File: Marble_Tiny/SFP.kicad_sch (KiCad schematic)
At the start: 73 parts, among them J1 TYCO_1888247-1, J11 TYCO_1888247-1, J12 TYCO_1888247-1, J13 TYCO_1888247-1, J8 2180739-1, J9 2180739-1, U17 TCA9535RTWR, U19 TCA9535RTWR, U26 PCA9546ARGV

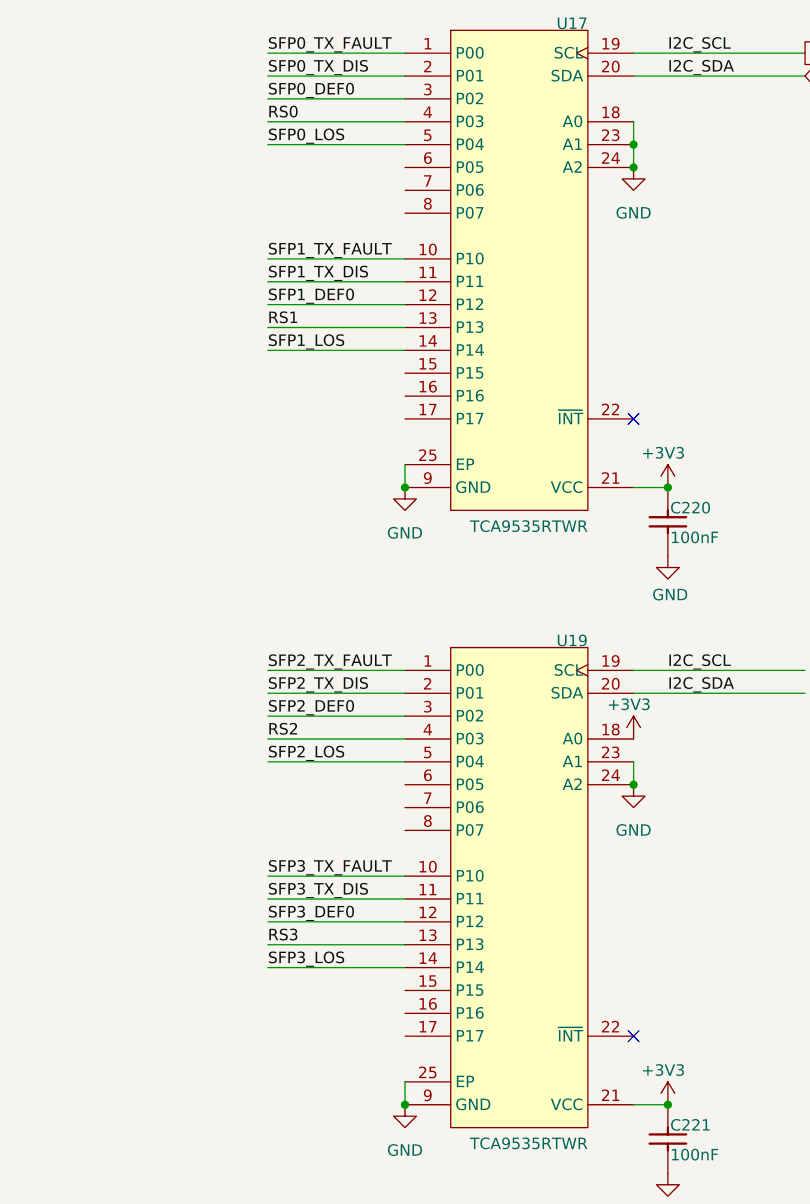
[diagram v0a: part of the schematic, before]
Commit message: fixed ERCs; added test points; added WP switch
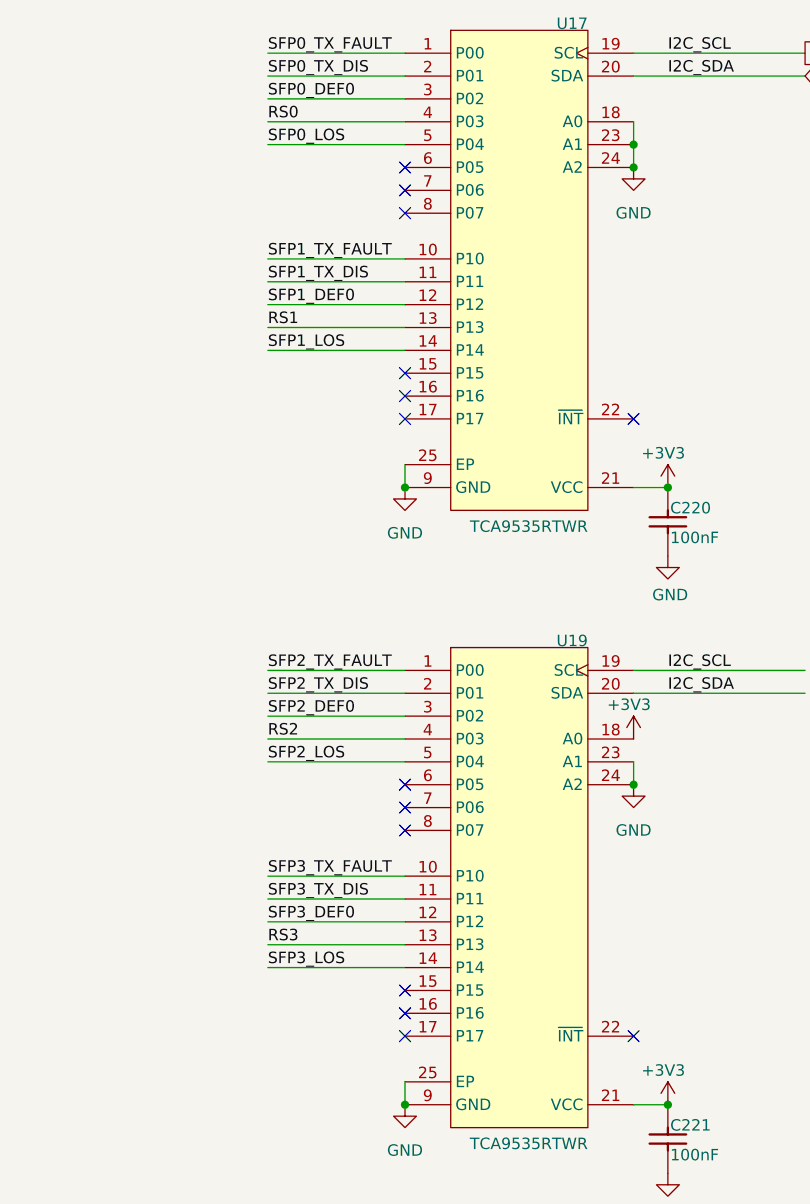
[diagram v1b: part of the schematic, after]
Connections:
- no-connect marks 3 -> 15
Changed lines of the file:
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@@
+	)
+	(no_connect
+		(at 323.85 115.57)
+	)
+	(no_connect
+		(at 323.85 110.49)
 	)
 	(no_connect
@@
 	)
 	(no_connect
+		(at 323.85 64.77)
+	)
+	(no_connect
+		(at 323.85 41.91)
+	)
+	(no_connect
+		(at 323.85 69.85)
+	)
+	(no_connect
+		(at 323.85 46.99)
+	)
+	(no_connect
+		(at 323.85 113.03)
+	)
+	(no_connect
 		(at 349.25 138.43)
+	)
+	(no_connect
+		(at 323.85 67.31)
+	)
+	(no_connect
+		(at 323.85 133.35)
+	)
+	(no_connect
+		(at 323.85 135.89)
+	)
+	(no_connect
+		(at 323.85 138.43)
 	)
 	(no_connect
 		(at 351.79 208.28)
 	)
+	(no_connect
+		(at 323.85 44.45)
+	)
 	(wire

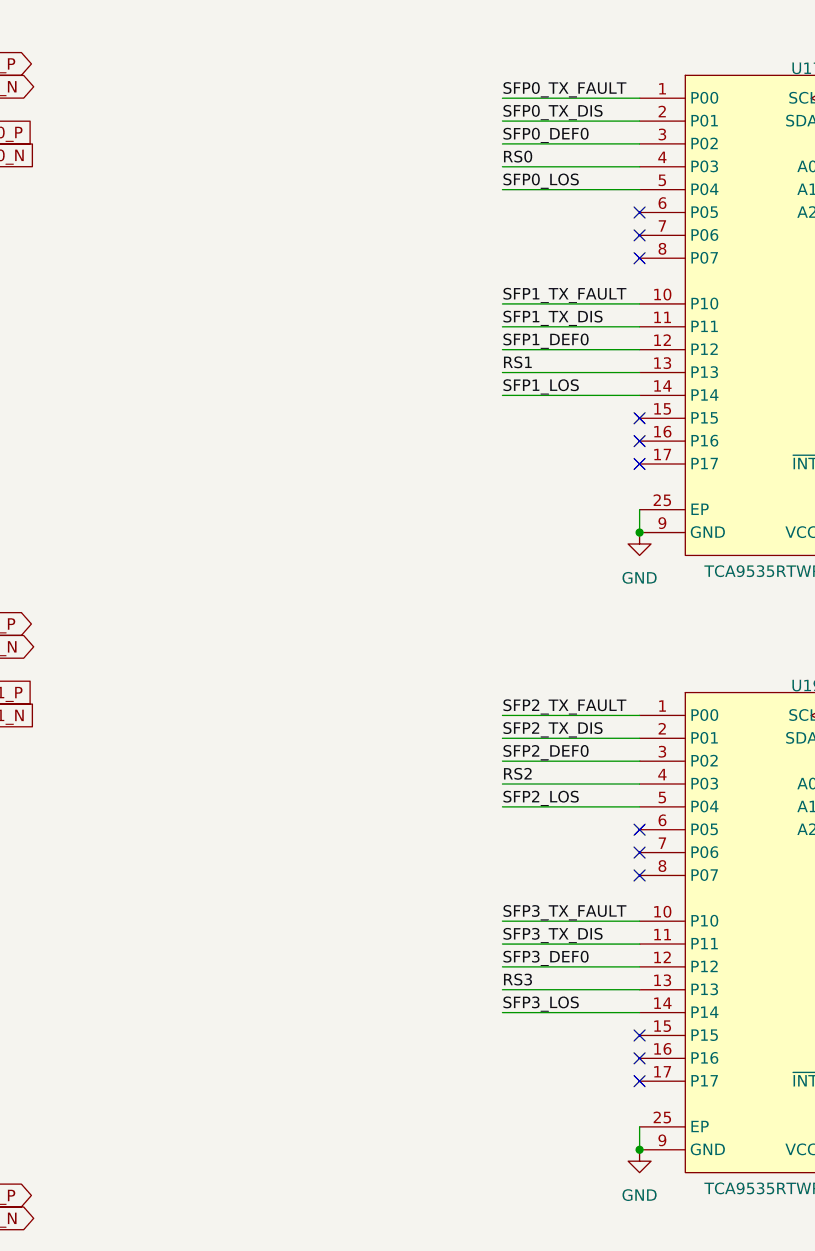
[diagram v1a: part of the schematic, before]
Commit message: fixed issue with PMODs; added board name and revision; fixed polygons issue
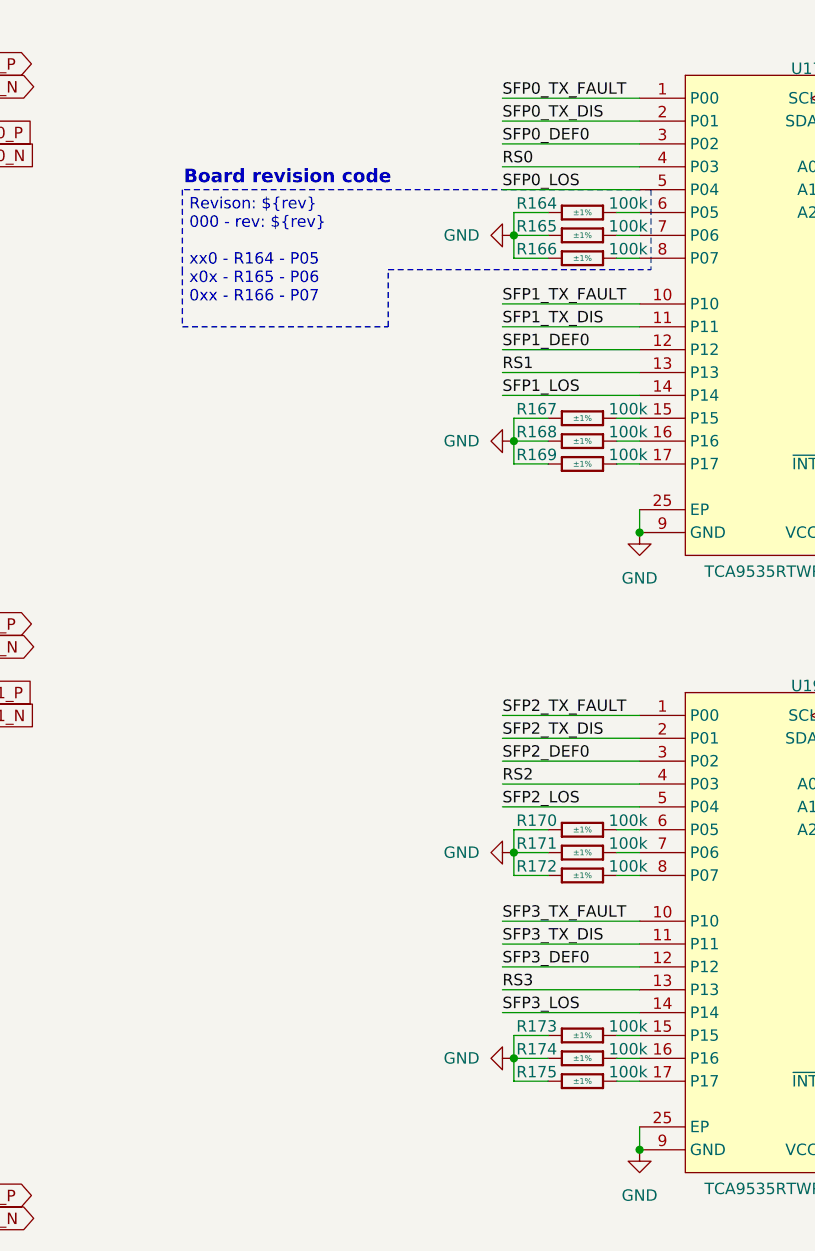
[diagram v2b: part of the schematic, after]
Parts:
- added R164, R165, R166, R167, R168, R169, R170, R171, R172, R173, R174, R175: R0402_100K_1%_0.0625W_100PPM, Resistors SMD:RESC1005X40N, symbol Resistors SMD:R0402_100K_1%_0.0625W_100PPM
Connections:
- net GND: now also R164.1, R165.1, R166.1, R167.1, R168.1, R169.1, R170.1, R171.1, R172.1, R173.1, R174.1, R175.1
- net at U17.15 (P15): now also R167.2
- net at U17.16 (P16): now also R168.2
- net at U17.17 (P17): now also R169.2
- net at U17.6 (P05): now also R164.2
- net at U17.7 (P06): now also R165.2
- net at U17.8 (P07): now also R166.2
- net at U19.15 (P15): now also R173.2
- net at U19.16 (P16): now also R174.2
- net at U19.17 (P17): now also R175.2
- net at U19.6 (P05): now also R170.2
- net at U19.7 (P06): now also R171.2
- net at U19.8 (P07): now also R172.2
- no-connect marks 15 -> 3
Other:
- note added: "Board revision code"
- note added: "Revison: ${rev} 000 - rev: ${rev} xx0 - R164 - P05 x0x - R165 - P06 0xx - R166 - P07"
- company: (none) -> ${name}
- title: (none) -> SFPs
